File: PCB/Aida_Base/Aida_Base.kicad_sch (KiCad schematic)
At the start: 232 parts, among them J1 AudioJack4, J10 Conn_01x03_Pin, J11 Conn_01x04_Pin, J12 Conn_01x04_Pin, J13 Conn_01x04_Pin, J14 Conn_01x04_Pin, J15 Conn_01x04_Pin, J16 Conn_01x04_Pin, J17 Conn_02x02_Odd_Even, J18 Conn_02x02_Odd_Even, J19 Conn_01x04_Pin, J2 AudioJack4, J20 Conn_01x06_Pin, J21 Conn_01x06_Pin, J22 Conn_01x04_Pin, J23 Conn_01x02_Pin, J24 Conn_01x02_Pin, J3 USB_C_Receptacle_L, J4 USB_C_Receptacle_R, J5 Conn_01x02_Pin, J6 Conn_01x02_Pin, J7 Conn_01x05_Pin, J8 Conn_01x05_Pin, J9 Conn_01x03_Pin, Q1 BSS138, Q2 BSS138, SW1 Boot, SW2 Boot, SW3 Reset, SW4 Reset, U3 RP2040_L, U4 RP2040_R, U5 W25Q128JVS, U6 W25Q128JVS, U7 AP2112K-3.3, U8 AP2112K-3.3, Y1 12MHz, Y2 12MHz

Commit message: 製造用出力
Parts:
- J3: value USB_C_Receptacle_L -> USB_C_Receptacle
- J4: value USB_C_Receptacle_R -> USB_C_Receptacle
- L1, L2, L3, L4, L5, L6, LS1, LS2, SW1, SW2, SW3, SW4: now left out of the parts list
- U3: value RP2040_L -> RP2040
- U4: value RP2040_R -> RP2040
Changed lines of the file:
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@@
 		(unit 1)
 		(exclude_from_sim no)
-		(in_bom yes)
+		(in_bom no)
 		(on_board yes)
 		(dnp no)
@@
 		(unit 1)
 		(exclude_from_sim no)
-		(in_bom yes)
+		(in_bom no)
 		(on_board yes)
 		(dnp no)
@@
 		(unit 1)
 		(exclude_from_sim no)
-		(in_bom yes)
+		(in_bom no)
 		(on_board yes)
 		(dnp no)
@@
 			)
 		)
-		(property "Value" "RP2040_L"
+		(property "Value" "RP2040"
 			(at 56.7533 207.3444 0)
 			(effects
@@
 		(unit 1)
 		(exclude_from_sim no)
-		(in_bom yes)
+		(in_bom no)
 		(on_board yes)
 		(dnp no)
@@
 		(unit 1)
 		(exclude_from_sim no)
-		(in_bom yes)
+		(in_bom no)
 		(on_board yes)
 		(dnp no)
@@
 		(unit 1)
 		(exclude_from_sim no)
-		(in_bom yes)
+		(in_bom no)
 		(on_board yes)
 		(dnp no)
@@
 		(unit 1)
 		(exclude_from_sim no)
-		(in_bom yes)
+		(in_bom no)
 		(on_board yes)
 		(dnp no)
@@
 		(unit 1)
 		(exclude_from_sim no)
-		(in_bom yes)
+		(in_bom no)
 		(on_board yes)
 		(dnp no)
@@
 		(unit 1)
 		(exclude_from_sim no)
-		(in_bom yes)
+		(in_bom no)
 		(on_board yes)
 		(dnp no)
@@
 		(unit 1)
 		(exclude_from_sim no)
-		(in_bom yes)
+		(in_bom no)
 		(on_board yes)
 		(dnp no)
@@
 		(unit 1)
 		(exclude_from_sim no)
-		(in_bom yes)
+		(in_bom no)
 		(on_board yes)
 		(dnp no)
@@
 			)
 		)
-		(property "Value" "USB_C_Receptacle_L"
+		(property "Value" "USB_C_Receptacle"
 			(at 109.22 111.3098 0)
 			(effects
@@
 			)
 		)
-		(property "Value" "RP2040_R"
+		(property "Value" "RP2040"
 			(at 254.8733 207.3444 0)
 			(effects
@@
 			)
 		)
-		(property "Value" "USB_C_Receptacle_R"
+		(property "Value" "USB_C_Receptacle"
 			(at 307.34 111.3098 0)
 			(effects
@@
 		(unit 1)
 		(exclude_from_sim no)
-		(in_bom yes)
+		(in_bom no)
 		(on_board yes)
 		(dnp no)

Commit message: フラッシュメモリのLCSC番号間違い修正
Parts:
- U5, U6: LCSC C190862 -> C97521
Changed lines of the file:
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@@
 			)
 		)
-		(property "LCSC" "C190862"
+		(property "LCSC" "C97521"
 			(at 41.91 229.87 0)
 			(effects
@@
 			)
 		)
-		(property "LCSC" "C190862"
+		(property "LCSC" "C97521"
 			(at 240.03 229.87 0)
 			(effects

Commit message: DN0020向けに回路図を更新
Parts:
- removed D1, D10, D11, D12, D13, D14, D15, D16, D17, D18, D19, D2, D20, D21, D22, D23, D24, D25, D26, D27, D28, D29, D3, D30, D31, D32, D33, D34, D35, D36, D37, D38, D39, D4, D40, D41, D42, D5, D6, D7, D8, D9: D, Lib_Local:D_SOD-123_Emphasized_Direction_Line, symbol Device:D
- removed H_btm_L3, H_btm_L4, H_btm_L5, H_btm_L6: GND_L, Lib_Local:MountingHole_M2_Through-hole_tap_TH-0.8-1.0-M2_minimal, symbol Mechanical:MountingHole_Pad
- removed H_btm_R3, H_btm_R4, H_btm_R5, H_btm_R6: GND_R, Lib_Local:MountingHole_M2_Through-hole_tap_TH-0.8-1.0-M2_minimal, symbol Mechanical:MountingHole_Pad
- removed H_mid_L1, H_mid_L2: GND_L_to_Mid, Lib_Local:MountingHole_M2_Through-hole_tap_TH-0.8-2.0-M2_minimal, symbol Mechanical:MountingHole_Pad
- removed H_mid_R1, H_mid_R2: GND_R_to_Mid, Lib_Local:MountingHole_M2_Through-hole_tap_TH-0.8-2.0-M2_minimal, symbol Mechanical:MountingHole_Pad
- removed J11, J12, J15, J16: Conn_01x04_Pin, Connector_PinHeader_1.00mm:PinHeader_1x04_P1.00mm_Vertical, symbol Connector:Conn_01x04_Pin
- removed J19, J22: Conn_01x04_Pin, Connector_PinHeader_2.00mm:PinHeader_1x04_P2.00mm_Vertical, symbol Connector:Conn_01x04_Pin
- removed J20, J21: Conn_01x06_Pin, Connector_PinHeader_2.00mm:PinHeader_1x06_P2.00mm_Vertical, symbol Connector:Conn_01x06_Pin
- removed J23, J24: Conn_01x02_Pin, Connector_PinHeader_2.00mm:PinHeader_1x02_P2.00mm_Vertical, symbol Connector:Conn_01x02_Pin
- removed J7, J8: Conn_01x05_Pin, Connector_PinHeader_1.00mm:PinHeader_1x05_P1.00mm_Vertical, symbol Connector:Conn_01x05_Pin
- removed JP1, JP2: SolderJumper_2_Open, Jumper:SolderJumper-2_P1.3mm_Open_RoundedPad1.0x1.5mm, symbol Jumper:SolderJumper_2_Open
- removed STLED1, STLED2: LED_GREEN, LED_SMD:LED_0201_0603Metric_Pad0.64x0.40mm_HandSolder, symbol Device:LED_Small
- removed SW_-1, SW_/1, SW_<1, SW_>1, SW_A1, SW_B1, SW_BS1, SW_C1, SW_CMD_L1, SW_CMD_R1, SW_CTL1, SW_D1, SW_E1, SW_ENT1, SW_F1, SW_I1, SW_J1, SW_K1, SW_L1, SW_M1, SW_N1, SW_O1, SW_OPT_L1, SW_OPT_R1, SW_S1, SW_SPC1, SW_V1, SW_W1, SW_X1, SW_Z1: SW_Push, Lib_Local:Kailh_socket_ChocV2_for_T=1.2mmPCB, symbol Switch:SW_Push
- removed SW_RE_L1, SW_RE_L2: RotaryEncoder_Switch, Lib_Local:ChocV2_AND_RotaryEncoder_Alps_EC11K-Switch_Vertical_H20mm_NPTH_MP_minimal, symbol Device:RotaryEncoder_Switch
- added C21, C24: 1u, Capacitor_SMD:C_0402_1005Metric, symbol Device:C_Small
- added J7, J8: Conn_01x04_Pin, Connector_PinHeader_2.54mm:PinHeader_1x04_P2.54mm_Vertical, symbol Connector:Conn_01x04_Pin
- added M1, M2: Motor_AC, symbol Motor:Motor_AC
- added SW10, SW11, SW12, SW13, SW14, SW15, SW16, SW17, SW18, SW19, SW20, SW21, SW22, SW23, SW24, SW25, SW26, SW27, SW28, SW29, SW30, SW31, SW32, SW33, SW34, SW5, SW6, SW7, SW8, SW9: SW_PUSH, Lib_Local:Kailh_socket_ChocV2_for_T=1.2mmPCB, symbol Switch:SW_Push_45deg
- added U1, U2: DRV2605LDGS, Package_SO:VSSOP-10_3x3mm_P0.5mm, symbol Driver_Haptic:DRV2605LDGS
- H1: renamed from H7; value COL_L_0_to_Mid_Outside -> KEY1
- H10: value MountingHole_Pad -> KEY_R5; now fitted
- H11: value COL_R_3_to_Mid -> KEY_R4
- H12: value COL_R_0_to_Mid_Outside -> KEY_R1
- H13: renamed from H15; value COL_L_4_to_Mid_Inside -> KEY10
- H14: value COL_R_4_from_Mid -> GND
- H15: renamed from H13; value COL_L_4_from_Mid_Inside -> GND
- H16: value COL_R_4_to_Mid/Top -> KEY_R10
- H17: renamed from H19; value COL_L_5_to_Mid_Inside -> KEY16
- H18: value COL_R_5_from_Mid -> GND
- H19: renamed from H17; value COL_L_5_from_Mid_Inside -> GND
- H2: renamed from H8; value COL_L_3_to_Mid_Inside -> KEY14
- H20: value COL_R_5_to_Mid -> KEY_R16
- H3: renamed from H9; value MountingHole_Pad -> KEY5; now fitted
- H4: value COL_R_4_from_Top -> GND
- H5: value COL_R_3_from_Mid -> GND
- H6: value COL_R_0_from_Mid_Outside -> GND
- H7: renamed from H1; value COL_L_0_from_Mid_Outside -> GND
- H8: renamed from H2; value COL_L_3_from_Mid_Inside -> GND
- H9: renamed from H3; value COL_L_4_from_Top -> GND
- R1, R2: value 1k -> R_Small; footprint Resistor_SMD:R_0402_1005Metric -> Lib_Local:Kailh_socket_ChocV2_for_T=1.2mmPCB; LCSC C11702 -> (none)
- R10, R11, R12, R13, R14, R15, R16, R17, R18, R19, R20, R21, R22, R27, R28, R29, R30, R5, R6, R7, R8, R9: footprint Resistor_SMD:R_0402_1005Metric -> Lib_Local:Kailh_socket_ChocV2_for_T=1.2mmPCB
- R23, R24, R25, R26: footprint Resistor_SMD:R_0402_1005Metric -> Lib_Local:Kailh_socket_ChocV2_for_T=1.2mmPCB; now fitted
- R3, R4: value 330 -> R_Small; footprint Resistor_SMD:R_0402_1005Metric -> Lib_Local:Kailh_socket_ChocV2_for_T=1.2mmPCB; LCSC C25104 -> (none)
- SD1, SD2: footprint Diode_SMD:D_SOD-123 -> Lib_Local:Kailh_socket_ChocV2_for_T=1.2mmPCB
- SW1, SW2, SW3, SW4: footprint Button_Switch_SMD:SW_SPST_PTS810 -> Lib_Local:Kailh_socket_ChocV2_for_T=1.2mmPCB
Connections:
- net GPIO00_L is gone; now on net KEY_L1: U3.2 (GPIO0)
- net GPIO00_R is gone; now on net KEY_R1: U4.2 (GPIO0)
- net GPIO22_L is gone; now on net SCL_L: U3.34 (GPIO22)
- net GPIO22_R is gone; now on net SCL_R: U4.34 (GPIO22)
- net GPIO23_L is gone; now on net SDA_L: U3.35 (GPIO23)
- net GPIO23_R is gone; now on net SDA_R: U4.35 (GPIO23)
- net GPIO24_L is gone; now on net DATA_L: U3.36 (GPIO24)
- net GPIO24_R is gone; now on net DATA_R: U4.36 (GPIO24)
- net GPIO27_L is gone; now on net GND_L: U3.39 (GPIO27/ADC1)
- net GPIO28_L is gone; now on net VBUS_DETECT_L: U3.40 (GPIO28/ADC2)
- net GPIO28_R is gone; now on net VBUS_DETECT_R: U4.40 (GPIO28/ADC2)
- net +3V3_L: now also U1.10 (VDD), U1.5 (EN), U1.6 (VDD/NC), U2.10 (VDD), U2.5 (EN), U2.6 (VDD/NC)
- net BUZZ_L: now also U3.31 (GPIO20); no longer U3.30 (GPIO19)
- net BUZZ_R: now also U4.31 (GPIO20); no longer U4.30 (GPIO19)
- net DATA_L: now also J1.R1; no longer R3.2, U3.17 (GPIO14)
- net DATA_R: now also J2.R1; no longer R4.2, U4.17 (GPIO14)
- net GND_L: now also H15.1, H19.1, H7.1, H8.1, H9.1, R4.2, C24.2, SW10.2, SW11.2, SW12.2, SW13.2, SW14.2, SW15.2, SW16.2, SW17.2, SW18.2, SW19.2, SW5.2, SW6.2, SW7.2, SW8.2, SW9.2, U1.4 (IN/TRIG), U1.8 (GND)
- net GND_R: now also R2.2, C21.2, U2.4 (IN/TRIG), U2.8 (GND)
- net SCL_L: now also J13.2 (Pin_2), R23.2, U1.2 (SCL); no longer J13.3 (Pin_3), R25.1, U3.32 (GPIO21)
- net SCL_R: now also J14.2 (Pin_2), R24.2, U2.2 (SCL); no longer J14.3 (Pin_3), R26.1, U4.32 (GPIO21)
- net SDA_L: now also J13.3 (Pin_3), R25.1, U1.3 (SDA); no longer J13.2 (Pin_2), R23.2, U3.31 (GPIO20)
- net SDA_R: now also J14.3 (Pin_3), R26.1, U2.3 (SDA); no longer J14.2 (Pin_2), R24.2, U4.31 (GPIO20)
- net VBUS_L: now also R3.1
- net VBUS_R: now also R1.1
- net at H4.1: now also H14.1, H18.1, H5.1, H6.1, SW20.2, SW21.2, SW22.2, SW23.2, SW24.2, SW25.2, SW26.2, SW27.2, SW28.2, SW29.2, SW30.2, SW31.2, SW32.2, SW33.2, SW34.2
- net VBUS_DETECT_R: now reaches R1.2
- net VBUS_DETECT_R: now also R2.1
- net VBUS_DETECT_L: now reaches R4.1
- net VBUS_DETECT_L: now also R3.2; no longer J2.R1
- net at U3.47 (USB_DP): now also R29.1; no longer R29.2
- net COL_L_0 renamed KEY_L1
- net KEY_L1: no longer U3.8 (GPIO6)
- net COL_L_1 renamed KEY_L8
- net KEY_L8: now also SW9.1
- net COL_L_2 renamed KEY_L9
- net KEY_L9: now also SW10.1
- net COL_L_3 renamed KEY_L10
- net KEY_L10: now also H13.1; no longer H2.1
- removed net COL_L_4: H13.1, H3.1, U3.13 (GPIO10)
- net COL_L_5 renamed KEY_L16
- net COL_R_0 renamed KEY_R1
- net KEY_R1: no longer U4.8 (GPIO6)
- net COL_R_1 renamed KEY_R8
- net KEY_R8: now also SW23.1
- net COL_R_2 renamed KEY_R9
- net KEY_R9: now also SW24.1
- net COL_R_3 renamed KEY_R10
- net KEY_R10: now also H16.1; no longer H11.1
- removed net COL_R_4: H10.1, H16.1, U4.13 (GPIO10)
- net COL_R_5 renamed KEY_R16
- net D_L+ renamed D+_L
- net D+_L: now also D43.3 (I/O2), R29.2; no longer D43.2 (I/O1), R29.1
- net D_L- renamed D-_L
- net D-_L: now also D43.2 (I/O1); no longer D43.3 (I/O2)
- net D_R+ renamed D+_R
- net D+_R: now also D44.3 (I/O2); no longer D44.2 (I/O1)
- net D_R- renamed D-_R
- net D-_R: now also D44.2 (I/O1); no longer D44.3 (I/O2)
- net ENC_L_A renamed KEY_L18
- net KEY_L18: now also SW17.1
- net ENC_L_B renamed KEY_L19
- net KEY_L19: now also SW18.1
- net ENC_R_A renamed KEY_R18
- net KEY_R18: now also SW26.1
- net ENC_R_B renamed KEY_R19
- net KEY_R19: now also SW33.1
- net GPIO01_L renamed KEY_L2
- net KEY_L2: now also SW5.1
- net GPIO01_R renamed KEY_R2
- net KEY_R2: now also SW21.1
- net GPIO11_L renamed KEY_L12
- net KEY_L12: now also SW12.1
- net GPIO11_R renamed KEY_R12
- net KEY_R12: now also SW29.1
- net GPIO12_L renamed KEY_L13
- net KEY_L13: now also SW13.1
- net GPIO12_R renamed KEY_R13
- net KEY_R13: now also SW28.1
- net GPIO13_L renamed KEY_L14
- net KEY_L14: now also SW14.1
- net GPIO13_R renamed KEY_R14
- net KEY_R14: now also SW25.1
- net GPIO25_L renamed RESERVE_L1
- net RESERVE_L1: now also J7.1 (Pin_1)
- net GPIO25_R renamed RESERVE_R1
- net RESERVE_R1: now also J8.1 (Pin_1)
- net GPIO26_L renamed RESERVE_L2
- net RESERVE_L2: now also J7.2 (Pin_2)
- net GPIO26_R renamed RESERVE_R2
- net RESERVE_R2: now also J8.2 (Pin_2)
- net GPIO27_R renamed RESERVE_R4
- net RESERVE_R4: now also J8.4 (Pin_4)
- net GPIO29_L renamed RESERVE_L3
- net RESERVE_L3: now also J7.3 (Pin_3)
- net GPIO29_R renamed RESERVE_R3
- net RESERVE_R3: now also J8.3 (Pin_3)
- net ROW_L_0 renamed KEY_L3
- net KEY_L3: now also SW6.1
- net ROW_L_1 renamed KEY_L4
- net KEY_L4: now also H2.1
- net ROW_L_2 renamed KEY_L5
- net KEY_L5: now also H3.1
- net ROW_L_3 renamed KEY_L6
- net KEY_L6: now also SW7.1
- net ROW_R_0 renamed KEY_R3
- net KEY_R3: now also SW20.1
- net ROW_R_1 renamed KEY_R4
- net KEY_R4: now also H11.1
- net ROW_R_2 renamed KEY_R5
- net KEY_R5: now also H10.1
- net ROW_R_3 renamed KEY_R6
- net KEY_R6: now also SW31.1
- new net: C24.1, U1.1 (REG)
- new net: M1.1, U1.7 (OUT+)
- new net: M1.2, U1.9 (OUT-)
- new net: C21.1, U2.1 (REG)
- new net: M2.1, U2.7 (OUT+)
- new net: M2.2, U2.9 (OUT-)
- new net KEY_L11: SW11.1, U3.13 (GPIO10)
- new net KEY_L15: SW15.1, U3.17 (GPIO14)
- new net KEY_L17: SW16.1, U3.32 (GPIO21)
- new net KEY_L20: SW19.1, U3.30 (GPIO19)
- new net KEY_L7: SW8.1, U3.8 (GPIO6)
- new net KEY_R11: SW30.1, U4.13 (GPIO10)
- new net KEY_R15: SW32.1, U4.17 (GPIO14)
- new net KEY_R17: SW27.1, U4.32 (GPIO21)
- new net KEY_R20: SW34.1, U4.30 (GPIO19)
- new net KEY_R7: SW22.1, U4.8 (GPIO6)
- no-connect marks 2 -> 3
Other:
- note added: "Buzzer"
- note added: "Debug"
- note added: "Flash memory"
- note added: "Haptic feedback"
- note added: "I2C"
- note added: "Key matrix"
- note added: "LED"
- note added: "MCU"
- note added: "Power"
- note added: "Reset & Boot"
- note added: "Split Handedness(*Left Only)"
- note added: "Transport"
- note added: "USB"
- note removed: "44PIN"
- note removed: "45PIN"
- note removed: "R3C5のスイッチは Midへ配置するかも"
- note removed: "SCREWS to Bottom Plate"
- note removed: "SCREWS to Mid"
- note removed: "TRRSに 保護回路が あってもよい"
- note removed: "Test Points"
- note removed: "Topへの Col4は 下のスイッチ と共通"
- note removed: "マトリクス内のMidねじ＝ボトム用ねじ の場合があるので、 こちらは少し減らす予定"
- moved on the sheet: C1, C10, C11, C12, C13, C14, C15, C16, C17, C18, C19, C2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

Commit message: フットプリント割り当て修正
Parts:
- R1, R10, R11, R12, R13, R14, R15, R16, R17, R18, R19, R2, R20, R21, R22, R23, R24, R25, R26, R27, R28, R29, R3, R30, R4, R5, R6, R7, R8, R9: footprint Lib_Local:Kailh_socket_ChocV2_for_T=1.2mmPCB -> Resistor_SMD:R_0402_1005Metric
- SD1, SD2: footprint Lib_Local:Kailh_socket_ChocV2_for_T=1.2mmPCB -> Diode_SMD:D_SOD-123
- SW1, SW2, SW3, SW4: footprint Lib_Local:Kailh_socket_ChocV2_for_T=1.2mmPCB -> Button_Switch_SMD:SW_SPST_PTS810
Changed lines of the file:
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@@
 			)
 		)
-		(property "Footprint" "Lib_Local:Kailh_socket_ChocV2_for_T=1.2mmPCB"
+		(property "Footprint" "Resistor_SMD:R_0402_1005Metric"
 			(at 339.09 213.36 0)
 			(effects
@@
 			)
 		)
-		(property "Footprint" "Lib_Local:Kailh_socket_ChocV2_for_T=1.2mmPCB"
+		(property "Footprint" "Resistor_SMD:R_0402_1005Metric"
 			(at 340.36 196.85 0)
 			(effects
@@
 			)
 		)
-		(property "Footprint" "Lib_Local:Kailh_socket_ChocV2_for_T=1.2mmPCB"
+		(property "Footprint" "Resistor_SMD:R_0402_1005Metric"
 			(at 375.92 240.03 0)
 			(effects
@@
 			)
 		)
-		(property "Footprint" "Lib_Local:Kailh_socket_ChocV2_for_T=1.2mmPCB"
+		(property "Footprint" "Resistor_SMD:R_0402_1005Metric"
 			(at 26.67 146.05 0)
 			(effects
@@
 			)
 		)
-		(property "Footprint" "Lib_Local:Kailh_socket_ChocV2_for_T=1.2mmPCB"
+		(property "Footprint" "Resistor_SMD:R_0402_1005Metric"
 			(at 171.45 265.43 0)
 			(effects
@@
 			)
 		)
-		(property "Footprint" "Lib_Local:Kailh_socket_ChocV2_for_T=1.2mmPCB"
+		(property "Footprint" "Resistor_SMD:R_0402_1005Metric"
 			(at 146.05 236.22 0)
 			(effects
@@
 			)
 		)
-		(property "Footprint" "Lib_Local:Kailh_socket_ChocV2_for_T=1.2mmPCB"
+		(property "Footprint" "Resistor_SMD:R_0402_1005Metric"
 			(at 139.7 233.68 0)
 			(effects
@@
 			)
 		)
-		(property "Footprint" "Lib_Local:Kailh_socket_ChocV2_for_T=1.2mmPCB"
+		(property "Footprint" "Resistor_SMD:R_0402_1005Metric"
 			(at 341.63 88.9 0)
 			(effects
@@
 			)
 		)
-		(property "Footprint" "Lib_Local:Kailh_socket_ChocV2_for_T=1.2mmPCB"
+		(property "Footprint" "Resistor_SMD:R_0402_1005Metric"
 			(at 218.44 40.64 0)
 			(effects
@@
 			)
 		)
-		(property "Footprint" "Lib_Local:Kailh_socket_ChocV2_for_T=1.2mmPCB"
+		(property "Footprint" "Resistor_SMD:R_0402_1005Metric"
 			(at 20.32 223.52 0)
 			(effects
@@
 			)
 		)
-		(property "Footprint" "Lib_Local:Kailh_socket_ChocV2_for_T=1.2mmPCB"
+		(property "Footprint" "Resistor_SMD:R_0402_1005Metric"
 			(at 26.67 186.69 0)
 			(effects
@@
 			)
 		)
-		(property "Footprint" "Lib_Local:Kailh_socket_ChocV2_for_T=1.2mmPCB"
+		(property "Footprint" "Resistor_SMD:R_0402_1005Metric"
 			(at 224.79 146.05 0)
 			(effects
@@
 			)
 		)
-		(property "Footprint" "Lib_Local:Kailh_socket_ChocV2_for_T=1.2mmPCB"
+		(property "Footprint" "Resistor_SMD:R_0402_1005Metric"
 			(at 138.43 175.26 0)
 			(effects
@@
 			)
 		)
-		(property "Footprint" "Lib_Local:Kailh_socket_ChocV2_for_T=1.2mmPCB"
+		(property "Footprint" "Resistor_SMD:R_0402_1005Metric"
 			(at 214.63 228.6 0)
 			(effects
@@
 			)
 		)
-		(property "Footprint" "Lib_Local:Kailh_socket_ChocV2_for_T=1.2mmPCB"
+		(property "Footprint" "Resistor_SMD:R_0402_1005Metric"
 			(at 224.79 148.59 0)
 			(effects
@@
 			)
 		)
-		(property "Footprint" "Lib_Local:Kailh_socket_ChocV2_for_T=1.2mmPCB"
+		(property "Footprint" "Resistor_SMD:R_0402_1005Metric"
 			(at 20.32 228.6 0)
 			(effects
@@
 			)
 		)
-		(property "Footprint" "Lib_Local:Kailh_socket_ChocV2_for_T=1.2mmPCB"
+		(property "Footprint" "Resistor_SMD:R_0402_1005Metric"
 			(at 130.81 88.9 0)
 			(effects
@@
 			)
 		)
-		(property "Footprint" "Lib_Local:Kailh_socket_ChocV2_for_T=1.2mmPCB"
+		(property "Footprint" "Resistor_SMD:R_0402_1005Metric"
 			(at 330.2 170.18 0)
 			(effects
@@
 			)
 		)
-		(property "Footprint" "Lib_Local:Kailh_socket_ChocV2_for_T=1.2mmPCB"
+		(property "Footprint" "Resistor_SMD:R_0402_1005Metric"
 			(at 19.05 48.26 0)
 			(effects
@@
 			)
 		)
-		(property "Footprint" "Lib_Local:Kailh_socket_ChocV2_for_T=1.2mmPCB"
+		(property "Footprint" "Button_Switch_SMD:SW_SPST_PTS810"
 			(at 284.48 228.6 0)
 			(effects
@@
 			)
 		)
-		(property "Footprint" "Lib_Local:Kailh_socket_ChocV2_for_T=1.2mmPCB"
+		(property "Footprint" "Button_Switch_SMD:SW_SPST_PTS810"
 			(at 87.63 227.33 0)
 			(effects
@@
 			)
 		)
-		(property "Footprint" "Lib_Local:Kailh_socket_ChocV2_for_T=1.2mmPCB"
+		(property "Footprint" "Button_Switch_SMD:SW_SPST_PTS810"
 			(at 284.48 224.79 0)
 			(effects
@@
 			)
 		)
-		(property "Footprint" "Lib_Local:Kailh_socket_ChocV2_for_T=1.2mmPCB"
+		(property "Footprint" "Resistor_SMD:R_0402_1005Metric"
 			(at 19.05 40.64 0)
 			(effects
@@
 			)
 		)
-		(property "Footprint" "Lib_Local:Kailh_socket_ChocV2_for_T=1.2mmPCB"
+		(property "Footprint" "Resistor_SMD:R_0402_1005Metric"
 			(at 341.63 91.44 0)
 			(effects
@@
 			)
 		)
-		(property "Footprint" "Lib_Local:Kailh_socket_ChocV2_for_T=1.2mmPCB"
+		(property "Footprint" "Button_Switch_SMD:SW_SPST_PTS810"
 			(at 87.63 223.52 0)
 			(effects
@@
 			)
 		)
-		(property "Footprint" "Lib_Local:Kailh_socket_ChocV2_for_T=1.2mmPCB"
+		(property "Footprint" "Diode_SMD:D_SOD-123"
 			(at 31.75 38.1 0)
 			(effects
@@
 			)
 		)
-		(property "Footprint" "Lib_Local:Kailh_socket_ChocV2_for_T=1.2mmPCB"
+		(property "Footprint" "Resistor_SMD:R_0402_1005Metric"
 			(at 138.43 200.66 0)
 			(effects
@@
 			)
 		)
-		(property "Footprint" "Lib_Local:Kailh_socket_ChocV2_for_T=1.2mmPCB"
+		(property "Footprint" "Resistor_SMD:R_0402_1005Metric"
 			(at 340.36 170.18 0)
 			(effects
@@
 			)
 		)
-		(property "Footprint" "Lib_Local:Kailh_socket_ChocV2_for_T=1.2mmPCB"
+		(property "Footprint" "Resistor_SMD:R_0402_1005Metric"
 			(at 128.27 175.26 0)
 			(effects
@@
 			)
 		)
-		(property "Footprint" "Lib_Local:Kailh_socket_ChocV2_for_T=1.2mmPCB"
+		(property "Footprint" "Resistor_SMD:R_0402_1005Metric"
 			(at 214.63 223.52 0)
 			(effects
@@
 			)
 		)
-		(property "Footprint" "Lib_Local:Kailh_socket_ChocV2_for_T=1.2mmPCB"
+		(property "Footprint" "Resistor_SMD:R_0402_1005Metric"
 			(at 218.44 48.26 0)
 			(effects
@@
 			)
 		)
-		(property "Footprint" "Lib_Local:Kailh_socket_ChocV2_for_T=1.2mmPCB"
+		(property "Footprint" "Resistor_SMD:R_0402_1005Metric"
 			(at 224.79 186.69 0)
 			(effects
@@
 			)
 		)
-		(property "Footprint" "Lib_Local:Kailh_socket_ChocV2_for_T=1.2mmPCB"
+		(property "Footprint" "Resistor_SMD:R_0402_1005Metric"
 			(at 345.44 215.9 0)
 			(effects
@@
 			)
 		)
-		(property "Footprint" "Lib_Local:Kailh_socket_ChocV2_for_T=1.2mmPCB"
+		(property "Footprint" "Diode_SMD:D_SOD-123"
 			(at 231.14 38.1 0)
 			(effects
@@
 			)
 		)
-		(property "Footprint" "Lib_Local:Kailh_socket_ChocV2_for_T=1.2mmPCB"
+		(property "Footprint" "Resistor_SMD:R_0402_1005Metric"
 			(at 130.81 91.44 0)
 			(effects
@@
 			)
 		)
-		(property "Footprint" "Lib_Local:Kailh_socket_ChocV2_for_T=1.2mmPCB"
+		(property "Footprint" "Resistor_SMD:R_0402_1005Metric"
 			(at 26.67 148.59 0)
 			(effects

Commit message: Hapticドライバまわりを修正
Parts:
- removed C21: 1u, Capacitor_SMD:C_0402_1005Metric, symbol Device:C_Small
- removed U2: DRV2605LDGS, Package_SO:VSSOP-10_3x3mm_P0.5mm, symbol Driver_Haptic:DRV2605LDGS
- added C29, C30, C32: 1u, Capacitor_SMD:C_0402_1005Metric, symbol Device:C_Small
- added U4: DRV2605LDGS, Package_SO:VSSOP-10_3x3mm_P0.5mm, symbol Driver_Haptic:DRV2605LDGS
- renumbered C14 to C10, C15 to C11, C16 to C12, C5 to C13, C6 to C14, C7 to C15, C8 to C16, C22 to C17, C23 to C18, C17 to C19, C18 to C20, C19 to C21, C20 to C22, C25 to C23, C26 to C24, C27 to C25, C28 to C26, C29 to C27, C30 to C28, C24 to C31, C35 to C33, C36 to C34, C37 to C35, C38 to C36, C31 to C37, C32 to C38, C33 to C39, C34 to C40, C10 to C5, C11 to C6, C12 to C7, C9 to C8, C13 to C9, D43 to D1, D44 to D2, D46 to D3, D45 to D4, H10 to H1, H7 to H10, H8 to H11, H9 to H12, H16 to H13, H13 to H14, H14 to H15, H15 to H16, H20 to H17, H17 to H18, H18 to H19, H11 to H2, H19 to H20, H12 to H3, H1 to H4, H2 to H5, H3 to H6, H4 to H7, H5 to H8, H6 to H9, J3 to J1, J7 to J10, J1 to J11, J8 to J12, J5 to J13, J6 to J14, J4 to J2, J14 to J3, J10 to J4, J13 to J5, J17 to J6, J18 to J7, J2 to J8, L4 to L1, L5 to L2, L6 to L3, L1 to L4, L2 to L5, L3 to L6, LS2 to LS1, LS1 to LS2, Q2 to Q1, Q1 to Q2, R3 to R1, R28 to R10, R29 to R11, R30 to R12, R11 to R15, R12 to R16, R15 to R17, R17 to R18, R18 to R19, R1 to R2, R16 to R20, R24 to R21, R26 to R22, R19 to R23, R20 to R24, R21 to R25, R22 to R26, R23 to R27, R25 to R28, R10 to R29, R4 to R3, R9 to R30, R2 to R4, R27 to R9, SW20 to SW1, SW8 to SW10, SW9 to SW11, SW10 to SW12, SW32 to SW13, SW25 to SW14, SW28 to SW15, SW29 to SW16, SW30 to SW17, SW11 to SW18, SW12 to SW19, SW21 to SW2, SW13 to SW20, SW14 to SW21, SW15 to SW22, SW34 to SW23, SW33 to SW24, SW26 to SW25, SW27 to SW26, SW16 to SW27, SW17 to SW28, SW18 to SW29, SW5 to SW3, SW19 to SW30, SW1 to SW31, SW2 to SW32, SW3 to SW33, SW4 to SW34, SW6 to SW4, SW24 to SW5, SW23 to SW6, SW22 to SW7, SW31 to SW8, SW7 to SW9, TP2 to TP1, TP1 to TP2, U7 to U1, U8 to U2, U1 to U3, U3 to U5, U4 to U6, U5 to U7, U6 to U8
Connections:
- net +3V3_L: now also C29.1
- net +3V3_R: now also C30.1, U4.10 (VDD), U4.5 (EN), U4.6 (VDD/NC)
- net GND_L: now also C29.2
- net GND_R: now also C30.2, C32.2, U4.4 (IN/TRIG), U4.8 (GND)
- net SCL_R: now also U4.2 (SCL)
- net SDA_R: now also U4.3 (SDA)
- net at M2.1: now also U4.7 (OUT+)
- net at M2.2: now also U4.9 (OUT-)
- new net: C32.1, U4.1 (REG)
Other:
- moved on the sheet: C31

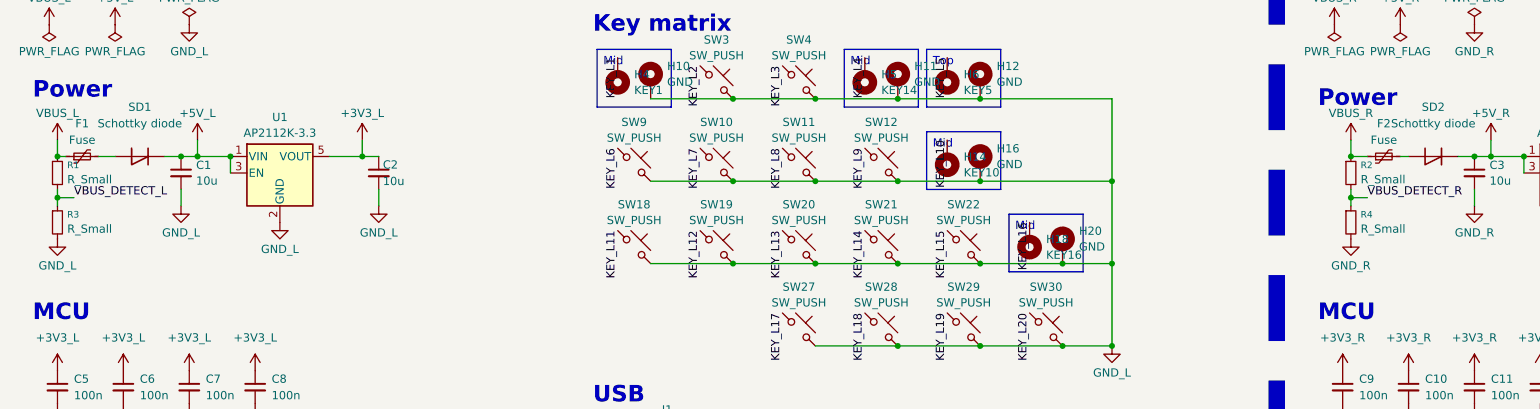
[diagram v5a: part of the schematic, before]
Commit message: VBUS検知の抵抗値を指定 #49
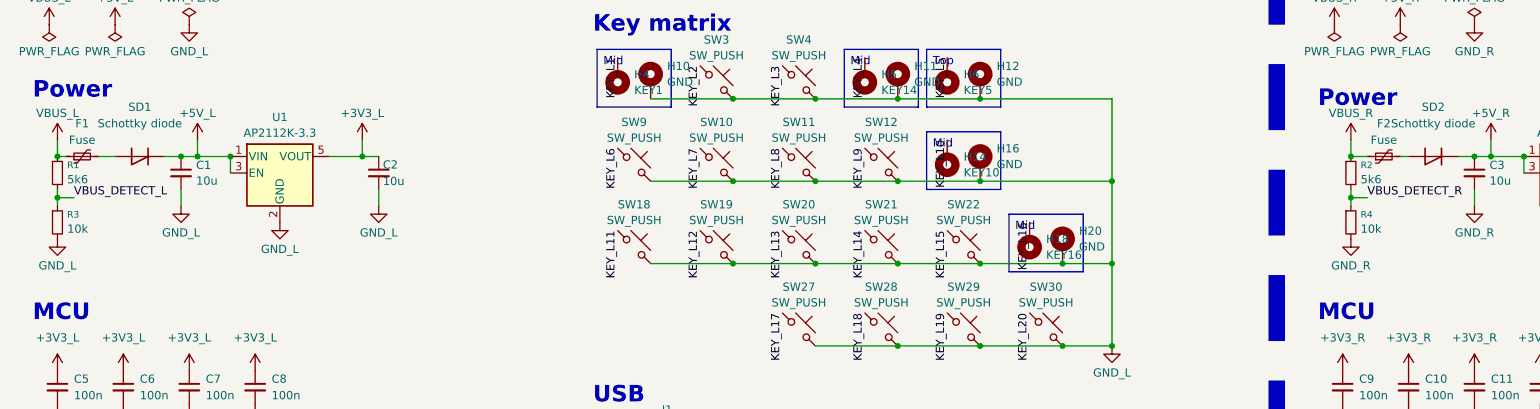
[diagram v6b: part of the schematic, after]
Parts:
- R1, R2: value R_Small -> 5k6
- R3, R4: value R_Small -> 10k
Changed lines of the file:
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@@
 			)
 		)
-		(property "Value" "R_Small"
+		(property "Value" "5k6"
 			(at 219.9386 41.6477 0)
 			(effects
@@
 			)
 		)
-		(property "Value" "R_Small"
+		(property "Value" "10k"
 			(at 20.5486 49.2677 0)
 			(effects
@@
 			)
 		)
-		(property "Value" "R_Small"
+		(property "Value" "5k6"
 			(at 20.5486 41.6477 0)
 			(effects
@@
 			)
 		)
-		(property "Value" "R_Small"
+		(property "Value" "10k"
 			(at 219.9386 49.2677 0)
 			(effects

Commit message: 左右判定ピンに左右別々の要素を割り当てた #52
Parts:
- removed J12: Conn_01x04_Pin, Connector_PinHeader_2.54mm:PinHeader_1x04_P2.54mm_Vertical, symbol Connector:Conn_01x04_Pin
- added J12: Conn_01x03_Pin, symbol Connector:Conn_01x03_Pin
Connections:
- net RESERVE_R4 is gone; now on net GND_R: U6.39 (GPIO27/ADC1)
- net +3V3_L: now also U5.39 (GPIO27/ADC1)
- net GND_L: no longer U5.39 (GPIO27/ADC1)
- net RESERVE_R1: now also J12.1 (Pin_1)
- net RESERVE_R2: now also J12.2 (Pin_2)
- net RESERVE_R3: now also J12.3 (Pin_3)
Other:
- note added: "Split Handedness(Left is High)"
- note added: "Split Handedness(Right is Low)"
- note removed: "Split Handedness(*Left Only)"

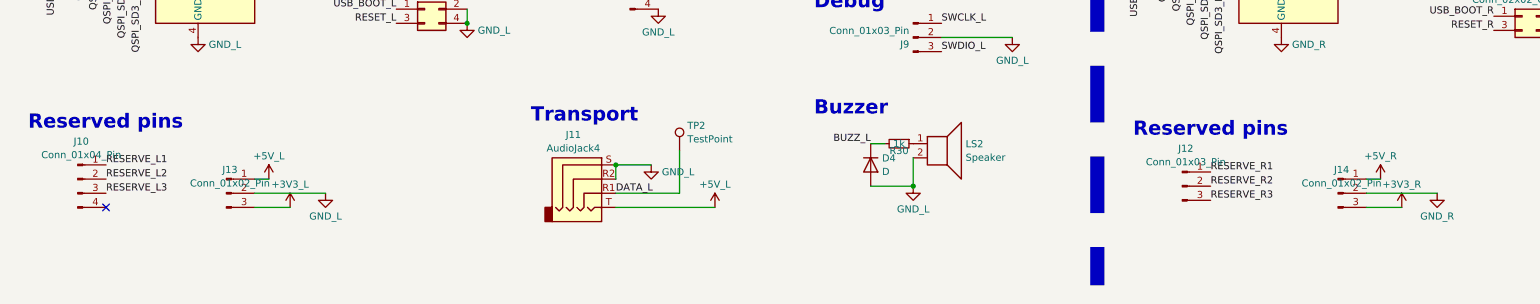
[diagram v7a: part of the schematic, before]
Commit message: VBUSをリザーブピンへ出した #50
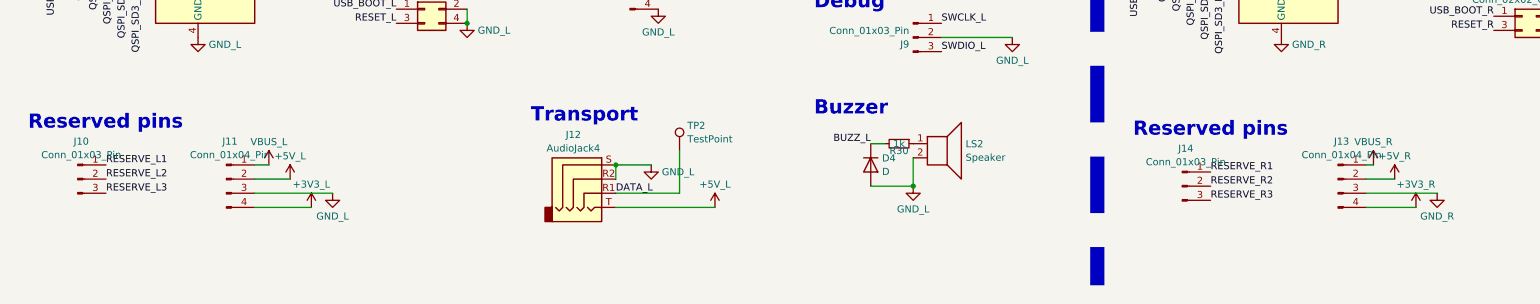
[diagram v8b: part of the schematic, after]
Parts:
- removed J10: Conn_01x04_Pin, Connector_PinHeader_2.54mm:PinHeader_1x04_P2.54mm_Vertical, symbol Connector:Conn_01x04_Pin
- removed J13, J14: Conn_01x02_Pin, Connector_PinHeader_2.00mm:PinHeader_1x03_P2.00mm_Vertical, symbol Connector:Conn_01x03_Pin
- added J10: Conn_01x03_Pin, symbol Connector:Conn_01x03_Pin
- added J11, J13: Conn_01x04_Pin, Connector_PinHeader_2.54mm:PinHeader_1x04_P2.54mm_Vertical, symbol Connector:Conn_01x04_Pin
- renumbered J11 to J12, J12 to J14
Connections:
- net +3V3_L: now also J11.4 (Pin_4)
- net +3V3_R: now also J13.4 (Pin_4)
- net +5V_L: now also J11.2 (Pin_2)
- net +5V_R: now also J13.2 (Pin_2)
- net GND_L: now also J11.3 (Pin_3)
- net GND_R: now also J13.3 (Pin_3)
- net RESERVE_L1: now also J10.1 (Pin_1)
- net RESERVE_L2: now also J10.2 (Pin_2)
- net RESERVE_L3: now also J10.3 (Pin_3)
- net VBUS_L: now also J11.1 (Pin_1)
- net VBUS_R: now also J13.1 (Pin_1)
- no-connect marks 3 -> 2
